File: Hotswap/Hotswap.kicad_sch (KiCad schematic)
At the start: 18 parts, among them J1 XT90PW-F, J2 XT90PW-F, J3 XT90PW-M, Q11 2N3904, Q2 IRFP4468PbF, Q4 IRFP4468PbF, Q8 IRFP4468PbF, Q9 IRFP4468PbF, U2 LM74800QDRRRQ1, U5 LM74800QDRRRQ1

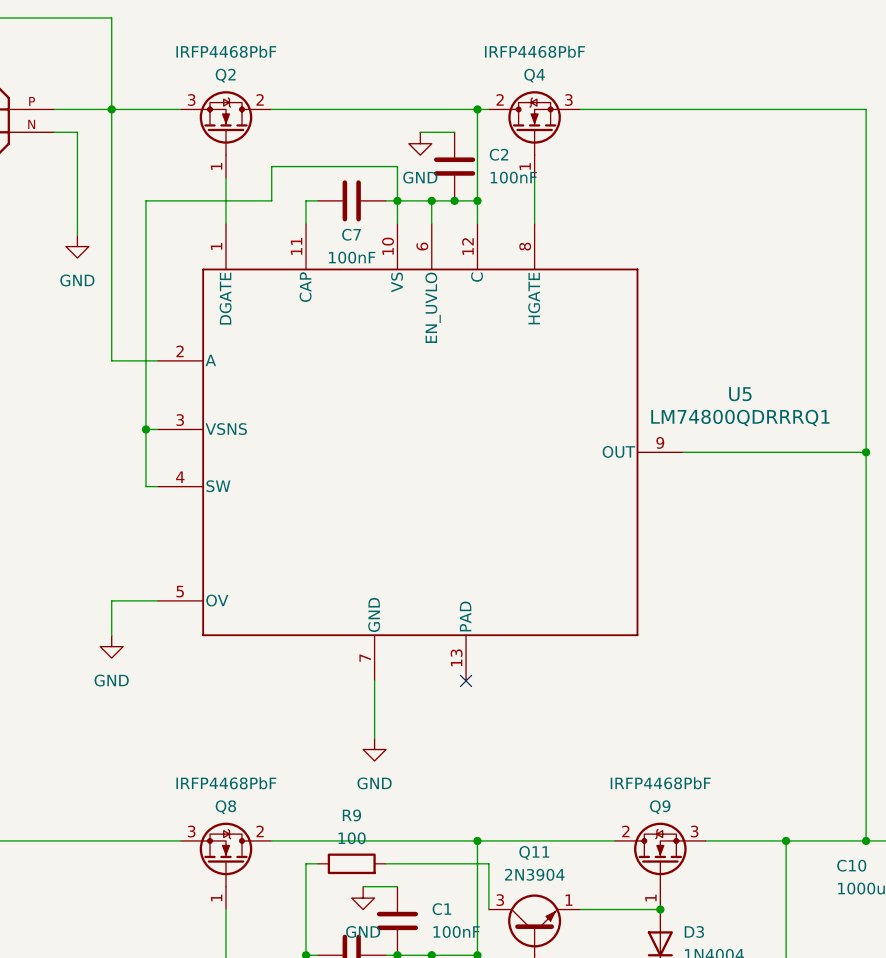
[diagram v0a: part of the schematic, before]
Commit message: update MOSFET to IRF7430
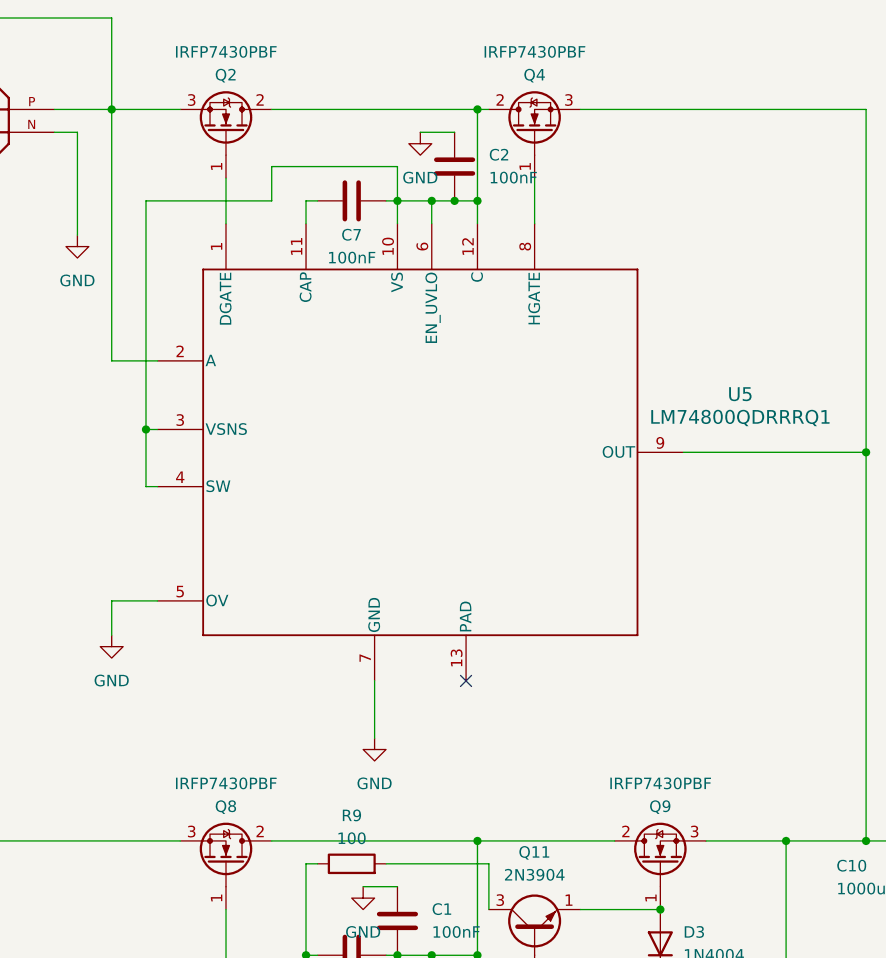
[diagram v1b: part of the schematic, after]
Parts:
- Q2, Q4, Q8, Q9: value IRFP4468PbF -> IRFP7430PBF; Link https://mou.sr/3w4O2Ob -> https://mou.sr/4j0VC0J; Mouser PN 726-IRFP4468PBFXKMA1 -> 942-IRFP7430PBF
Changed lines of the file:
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@@
 			)
 		)
-		(property "Value" "IRFP4468PbF"
+		(property "Value" "IRFP7430PBF"
 			(at 149.86 101.6 90)
 			(effects
@@
 			)
 		)
-		(property "Link" "https://mou.sr/3w4O2Ob"
+		(property "Link" "https://mou.sr/4j0VC0J"
 			(at 149.86 110.49 90)
 			(effects
@@
 			)
 		)
-		(property "Mouser PN" "726-IRFP4468PBFXKMA1 "
+		(property "Mouser PN" "942-IRFP7430PBF "
 			(at 149.86 110.49 90)
 			(effects
@@
 			)
 		)
-		(property "Value" "IRFP4468PbF"
+		(property "Value" "IRFP7430PBF"
 			(at 101.6 20.32 90)
 			(effects
@@
 			)
 		)
-		(property "Link" "https://mou.sr/3w4O2Ob"
+		(property "Link" "https://mou.sr/4j0VC0J"
 			(at 101.6 29.21 90)
 			(effects
@@
 			)
 		)
-		(property "Mouser PN" "726-IRFP4468PBFXKMA1 "
+		(property "Mouser PN" "942-IRFP7430PBF "
 			(at 101.6 29.21 90)
 			(effects
@@
 			)
 		)
-		(property "Value" "IRFP4468PbF"
+		(property "Value" "IRFP7430PBF"
 			(at 135.89 20.32 90)
 			(effects
@@
 			)
 		)
-		(property "Link" "https://mou.sr/3w4O2Ob"
+		(property "Link" "https://mou.sr/4j0VC0J"
 			(at 135.89 29.21 90)
 			(effects
@@
 			)
 		)
-		(property "Mouser PN" "726-IRFP4468PBFXKMA1 "
+		(property "Mouser PN" "942-IRFP7430PBF "
 			(at 135.89 29.21 90)
 			(effects
@@
 			)
 		)
-		(property "Value" "IRFP4468PbF"
+		(property "Value" "IRFP7430PBF"
 			(at 101.6 101.6 90)
 			(effects
@@
 			)
 		)
-		(property "Link" "https://mou.sr/3w4O2Ob"
+		(property "Link" "https://mou.sr/4j0VC0J"
 			(at 101.6 110.49 90)
 			(effects
@@
 			)
 		)
-		(property "Mouser PN" "726-IRFP4468PBFXKMA1 "
+		(property "Mouser PN" "942-IRFP7430PBF "
 			(at 101.6 110.49 90)
 			(effects
